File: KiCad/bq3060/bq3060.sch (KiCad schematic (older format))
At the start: 68 parts, among them Q1 Si1023x, Q2 Si1023x, Q3 NDS351AN, Q4 SI4435DYTRPBF, Q5 SI4435DYTRPBF, Q6 SI4435DYTRPBF, U1 BQ29412DCT, U2 BQ3060PW

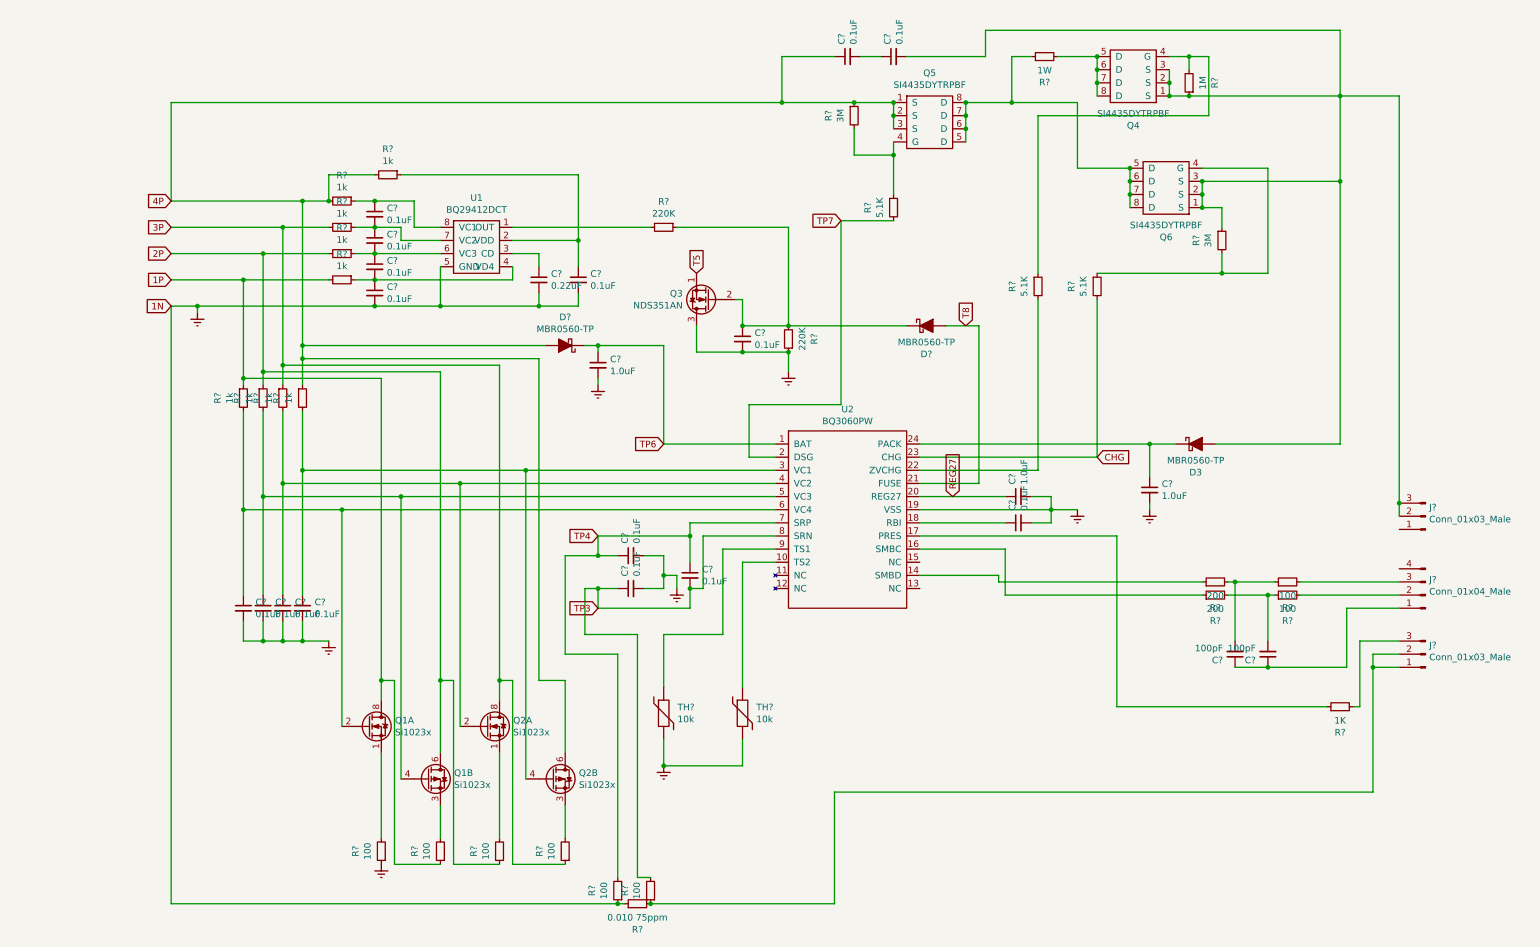
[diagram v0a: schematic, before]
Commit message: Finish bq3060 schematic
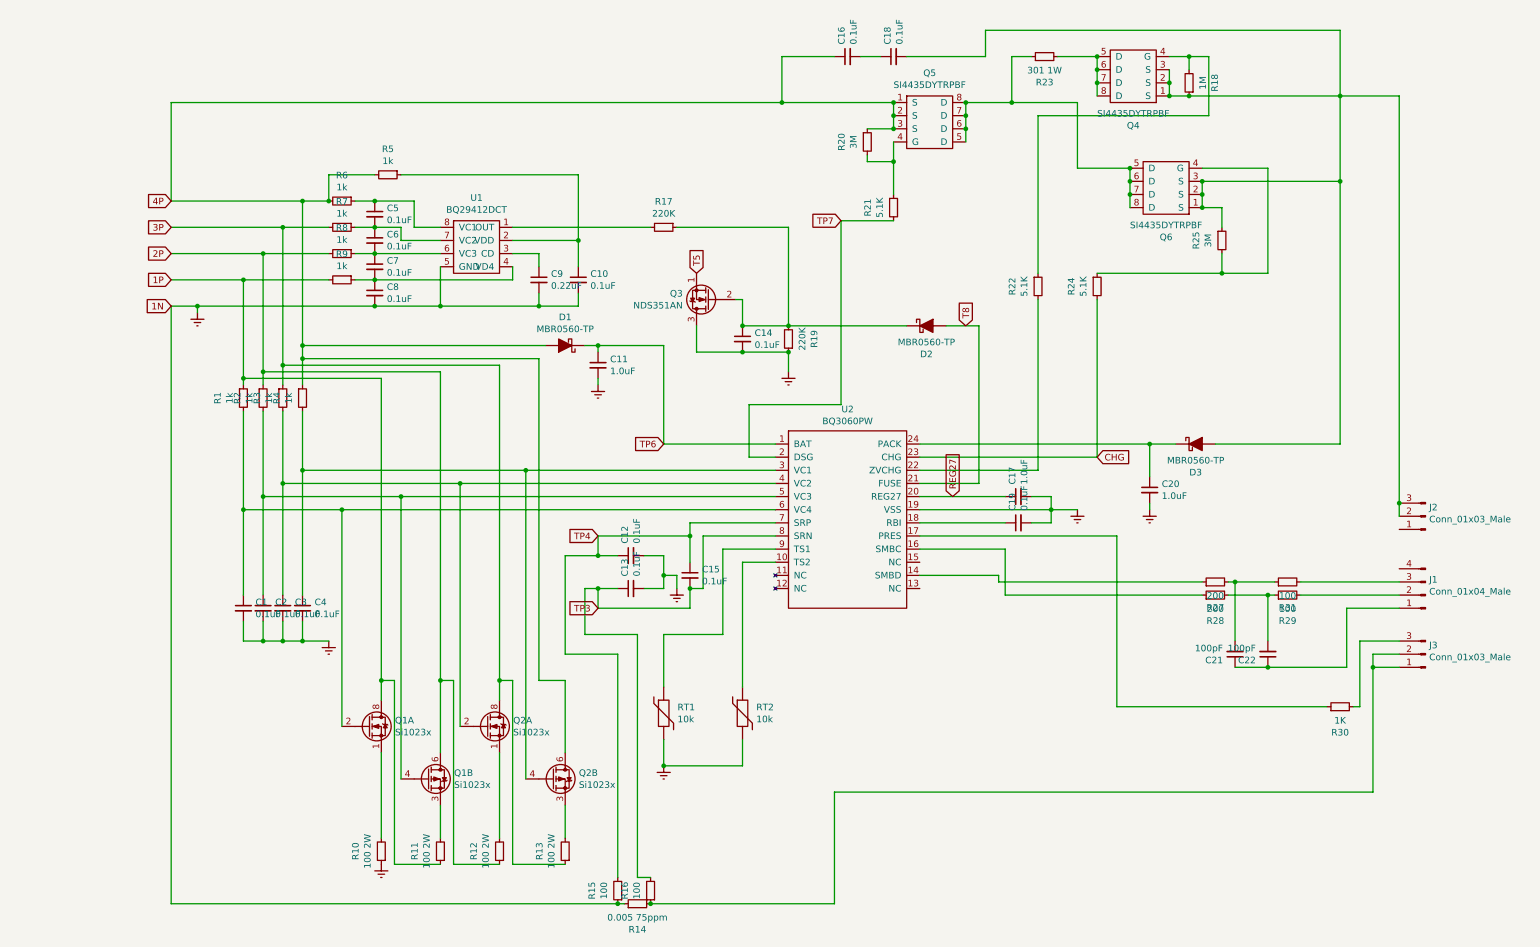
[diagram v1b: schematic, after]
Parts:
- C1, C10, C11, C12, C13, C14, C15, C16, C17, C18, C19, C2, C20, C21, C22, C3, C4, C5, C6, C7, C8, C9: renamed from C?; footprint (none) -> Capacitor_SMD:C_0805_2012Metric_Pad1.15x1.40mm_HandSolder
- D1, D2: renamed from D?; footprint (none) -> Diode_SMD:D_SOD-123
- D3: footprint (none) -> Diode_SMD:D_SOD-123
- J1: renamed from J?; footprint (none) -> Connector_PinHeader_2.54mm:PinHeader_1x04_P2.54mm_Horizontal
- J2, J3: renamed from J?; footprint (none) -> Connector_PinHeader_2.54mm:PinHeader_1x03_P2.54mm_Vertical
- Q4, Q5, Q6: footprint (none) -> Package_SO:SOIC-8_3.9x4.9mm_P1.27mm
- R1, R15, R16, R17, R18, R19, R2, R20, R21, R22, R24, R25, R27, R28, R29, R3, R30, R31, R4, R5, R6, R7, R8, R9: renamed from R?; footprint (none) -> Resistor_SMD:R_0805_2012Metric_Pad1.15x1.40mm_HandSolder
- R10, R11, R12, R13: renamed from R?; value 100 -> 100 2W; footprint (none) -> Resistor_SMD:R_2512_6332Metric_Pad1.52x3.35mm_HandSolder
- R14: renamed from R?; value 0.010 75ppm -> 0.005 75ppm; footprint (none) -> Resistor_SMD:R_2512_6332Metric_Pad1.52x3.35mm_HandSolder
- R23: renamed from R?; value 1W -> 301 1W; footprint (none) -> Resistor_SMD:R_2512_6332Metric_Pad1.52x3.35mm_HandSolder
- RT1, RT2: renamed from TH?; footprint (none) -> Resistor_SMD:R_0805_2012Metric_Pad1.15x1.40mm_HandSolder
- U1: footprint (none) -> footprints:SN74LVC2G241_DCT_8
- U2: footprint (none) -> Package_SO:TSSOP-24_4.4x7.8mm_P0.65mm
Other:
- moved on the sheet: R20

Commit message: Routing attempt
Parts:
- added J4: Conn_01x03_Male, Connector_Wire:SolderWirePad_1x03_P5.715mm_Drill2mm, symbol Connector:Conn_01x03_Male
- added J5: Conn_01x02_Male, Connector_Wire:SolderWirePad_1x02_P7.62mm_Drill2mm, symbol Connector:Conn_01x02_Male
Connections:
- net 1P: now also J5.1 (Pin_1)
- net 2P: now also J4.3 (Pin_3)
- net 3P: now also J4.2 (Pin_2)
- net 4P: now also J4.1 (Pin_1)
- net Earth: now also J5.2 (Pin_2)
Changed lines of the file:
@@
 Wire Wire Line
 	5050 7000 5000 7000
+Text GLabel 850  1400 2    50   Input ~ 0
+4P
+Text GLabel 850  1500 2    50   Input ~ 0
+3P
+Text GLabel 850  1600 2    50   Input ~ 0
+2P
+Text GLabel 850  1850 2    50   Input ~ 0
+1P
+Text GLabel 850  1950 2    50   Input ~ 0
+1N
+$Comp
+L Connector:Conn_01x03_Male J4
+U 1 1 60B8AEED
+P 650 1500
+F 0 "J4" H 758 1781 50  0000 C CNN
+F 1 "Conn_01x03_Male" H 758 1690 50  0000 C CNN
+F 2 "Connector_Wire:SolderWirePad_1x03_P5.715mm_Drill2mm" H 650 1500 50  0001 C CNN
+F 3 "~" H 650 1500 50  0001 C CNN
+	1    650  1500
+	1    0    0    -1
+$EndComp
+$Comp
+L Connector:Conn_01x02_Male J5
+U 1 1 60B8B6CD
+P 650 1850
+F 0 "J5" H 758 2031 50  0000 C CNN
+F 1 "Conn_01x02_Male" H 758 1940 50  0000 C CNN
+F 2 "Connector_Wire:SolderWirePad_1x02_P7.62mm_Drill2mm" H 650 1850 50  0001 C CNN
+F 3 "~" H 650 1850 50  0001 C CNN
+	1    650  1850
+	1    0    0    -1
+$EndComp
 $EndSCHEMATC

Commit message: Add prototype bq3060 design
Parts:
- Q3: footprint Package_TO_SOT_THT:TO-92_Inline -> Package_TO_SOT_SMD:SOT-23
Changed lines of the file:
@@
 F 0 "Q3" H 5905 2354 50  0000 L CNN
 F 1 "NDS351AN" H 5905 2445 50  0000 L CNN
-F 2 "Package_TO_SOT_THT:TO-92_Inline" H 5900 2325 50  0001 L CIN
+F 2 "Package_TO_SOT_SMD:SOT-23" H 5900 2325 50  0001 L CIN
 F 3 "https://www.fairchildsemi.com/datasheets/2N/2N7000.pdf" H 5700 2400 50  0001 L CNN
 	1    5700 2400
